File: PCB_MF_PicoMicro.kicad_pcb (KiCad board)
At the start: 2 copper layers, 36.5 x 18.5 mm, 45 parts, among them J1 Conn_01x12, J2 Conn_01x12, J3 USB_C_Receptacle_USB2.0_16P, J7 Conn_01x02_Pin, J8 Conn_01x02_Pin, SW1 SW_Push, U1 RP2040, U2 AMS1117-3.3, U4 W25Q16JVSS, Y1 X322512MSB4SI

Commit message: update production files
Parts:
- C11, C12, C13, C14, C15, C6, C9: value 100n -> 100nF
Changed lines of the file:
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@@
 			)
 		)
-		(property "Value" "100n"
+		(property "Value" "100nF"
 			(at 0 1.16 270)
 			(layer "F.Fab")
@@
 			)
 		)
-		(property "Value" "100n"
+		(property "Value" "100nF"
 			(at 0 1.16 180)
 			(layer "F.Fab")
@@
 			)
 		)
-		(property "Value" "100n"
+		(property "Value" "100nF"
 			(at 0 1.16 0)
 			(layer "F.Fab")
@@
 			)
 		)
-		(property "Value" "100n"
+		(property "Value" "100nF"
 			(at 0 1.16 0)
 			(layer "F.Fab")
@@
 			)
 		)
-		(property "Value" "100n"
+		(property "Value" "100nF"
 			(at 0 1.16 0)
 			(layer "F.Fab")
@@
 			)
 		)
+		(property "LCSC" "C25076"
+			(at 0 0 0)
+			(layer "F.SilkS")
+			(hide yes)
+			(effects
+				(font
+					(size 1.27 1.27)
+					(thickness 0.15)
+				)
+			)
+		)
 		(property ki_fp_filters "R_*")
 		(sheetname "/")
@@
 			)
 		)
-		(property "Value" "100n"
+		(property "Value" "100nF"
 			(at 0 1.16 0)
 			(layer "F.Fab")
@@
 			)
 		)
+		(property "LCSC" "C25076"
+			(at 0 0 0)
+			(layer "F.SilkS")
+			(hide yes)
+			(effects
+				(font
+					(size 1.27 1.27)
+					(thickness 0.15)
+				)
+			)
+		)
 		(property ki_fp_filters "R_*")
 		(sheetname "/")
@@
 			)
 		)
-		(property "Value" "100n"
+		(property "Value" "100nF"
 			(at 0 1.16 0)
 			(layer "F.Fab")

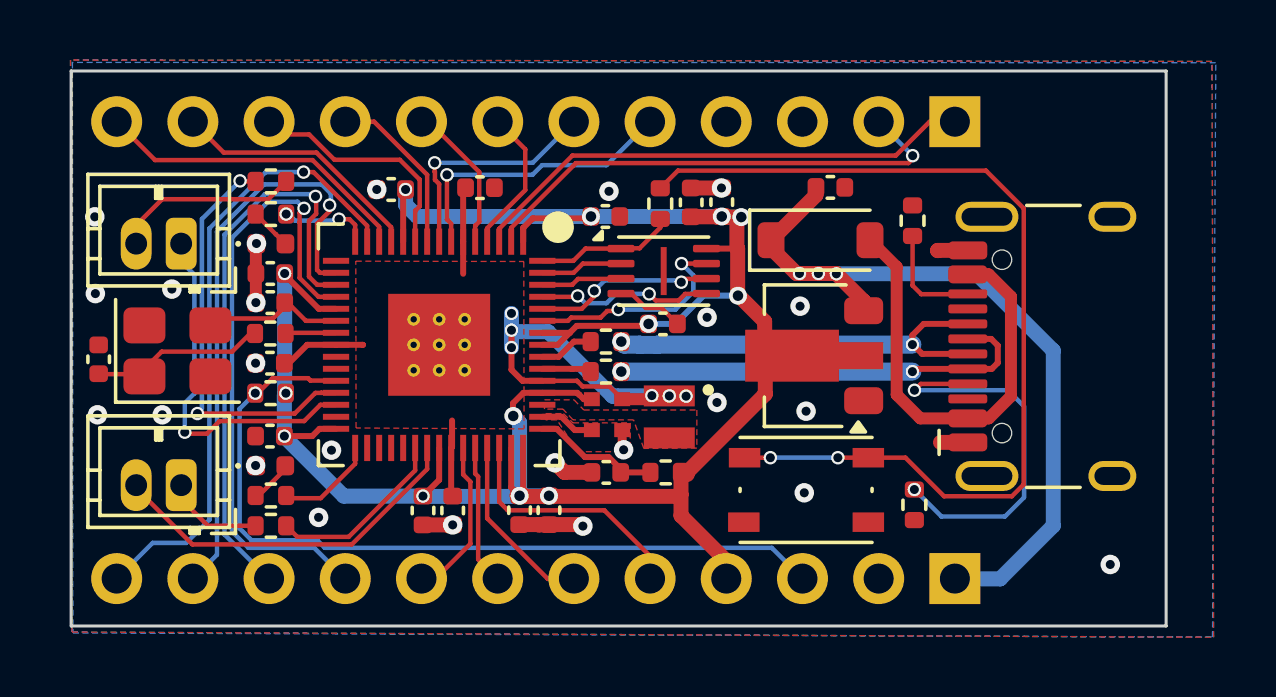
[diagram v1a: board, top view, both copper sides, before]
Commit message: swap tx line to slave, better arrangement of parts
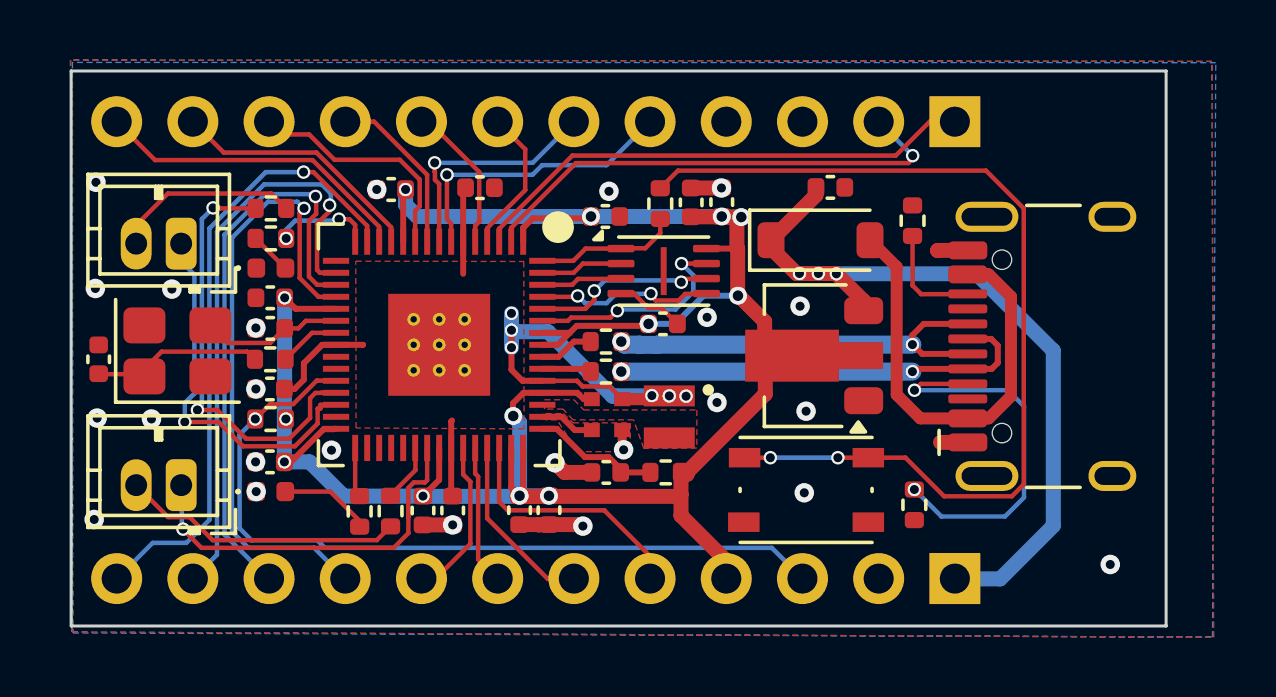
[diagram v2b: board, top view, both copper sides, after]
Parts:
- moved R12 4.02 mm to (115.9, 96.1), turned to 90 degrees
- moved R10 3.01 mm to (114.8, 96.1), turned to 90 degrees
- moved R11 0.90 mm to (111.9, 86.0)
- moved C12 0.86 mm to (111.9, 94.5)
- moved C4 0.86 mm to (111.9, 90.0)
- moved C7 0.86 mm to (111.9, 92.0)
- moved D2 0.86 mm to (111.9, 95.4)
- moved R2 0.86 mm to (111.9, 91.0)
- moved R6 0.86 mm to (111.9, 93.0)
- moved C9 0.81 mm to (111.9, 89.0)
- moved R9 0.81 mm to (111.9, 87.0)
- moved D3 0.81 mm to (111.9, 88.0)
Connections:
- J8 pad 1: Net-(J8-Pin_1) -> RX2
- J8 pad 2: RX2 -> Net-(J8-Pin_2)
- R12 pad 1: Net-(J8-Pin_1) -> Net-(J8-Pin_2)
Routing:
- net Net-(J8-Pin_2): track 0.00 -> 10.4 mm
- net TX2: track 6.12 -> 1.94 mm
- net Net-(J8-Pin_1): track 3.52 -> 0.00 mm
- net GND: track 15.8 -> 13.8 mm
- net /RP2350A/GPIO19: track 3.25 -> 1.67 mm
- net Net-(D2-A): track 1.56 -> 3.08 mm
- net RX2: track 12.6 -> 13.5 mm, vias 0 -> 1
- net TX1: track 13.8 -> 14.6 mm
- net +1V1: track 23.6 -> 24.3 mm
- net RST: track 27.6 -> 27.0 mm
- net RX1: track 12.2 -> 12.7 mm

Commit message: better positioning of parts
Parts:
- R11, R12: value 100 -> 50
- moved R6 3.63 mm to (113.8, 96.1), turned to -90 degrees
- moved D3 2.48 mm to (111.9, 85.5)
- moved R11 1.52 mm to (111.9, 87.5)
- moved C12 1.40 mm to (111.9, 93.0)
- moved D2 1.40 mm to (111.9, 94.0)
- moved R8 1.32 mm to (132.5, 85.3), turned to 0 degrees
- moved C7 0.55 mm to (111.9, 91.5)
- moved R2 0.54 mm to (111.9, 90.5)
- moved C4 0.50 mm to (111.9, 89.5)
- moved R9 0.49 mm to (111.9, 86.5)
- moved C9 0.47 mm to (111.9, 88.5)
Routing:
- net Net-(J3-CC2): track 3.61 -> 14.1 mm, vias 0 -> 2
- net RST: track 27.0 -> 32.2 mm
- net /RP2350A/~{USB_BOOT}: track 32.2 -> 35.1 mm
- net RX2: track 13.5 -> 16.3 mm
- net TX1: track 14.6 -> 12.5 mm
- net Net-(D2-A): track 3.08 -> 4.52 mm
- net Net-(J7-Pin_2): track 6.27 -> 7.60 mm
- net VIN: track 26.2 -> 25.2 mm
- net +1V1: track 24.3 -> 23.6 mm
- net Net-(J8-Pin_2): track 10.4 -> 10.9 mm
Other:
- board text removed: "D7"

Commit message: update production files
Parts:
- U1: value RP2040 -> RP2350A
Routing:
- net GND: vias 24 -> 23
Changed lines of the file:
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@@
 			)
 		)
-		(property "LCSC" "C25076"
+		(property "LCSC" "C25120"
 			(at 0 0 0)
 			(layer "F.SilkS")
@@
 			)
 		)
-		(property "LCSC" "C25076"
+		(property "LCSC" "C25120"
 			(at 0 0 90)
 			(layer "F.SilkS")
@@
 			)
 		)
-		(property "Value" "RP2040"
+		(property "Value" "RP2350A"
 			(at 0 5.55 90)
 			(layer "F.Fab")
@@
 	)
 	(gr_text "PicoMicroMS\nV1.1\n??/25"
-		(at 136.5 92.36 0)
+		(at 136.5 92.81 0)
 		(layer "B.SilkS")
 		(effects
@@
 		(size 0.65)
 		(drill 0.3)
-		(layers "F.Cu" "B.Cu")
-		(net 2)
-	)
-	(via
-		(at 139.87 97.87)
-		(size 0.65)
-		(drill 0.3)

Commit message: add SDA and SCL markings
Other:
- board text added: "SCL/D3"
- board text added: "SDA/D2"
- board text removed: "D2"
- board text removed: "D3"
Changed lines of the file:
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@@
 		)
 	)
-	(gr_text "D2"
-		(at 123.8 86.574762 270)
+	(gr_text "SDA/D2"
+		(at 123.86 90.44 270)
 		(layer "B.SilkS")
 		(effects
@@
 		)
 	)
-	(gr_text "D3"
-		(at 121.3 86.574762 270)
+	(gr_text "SCL/D3"
+		(at 121.28 90.34 270)
 		(layer "B.SilkS")
 		(effects

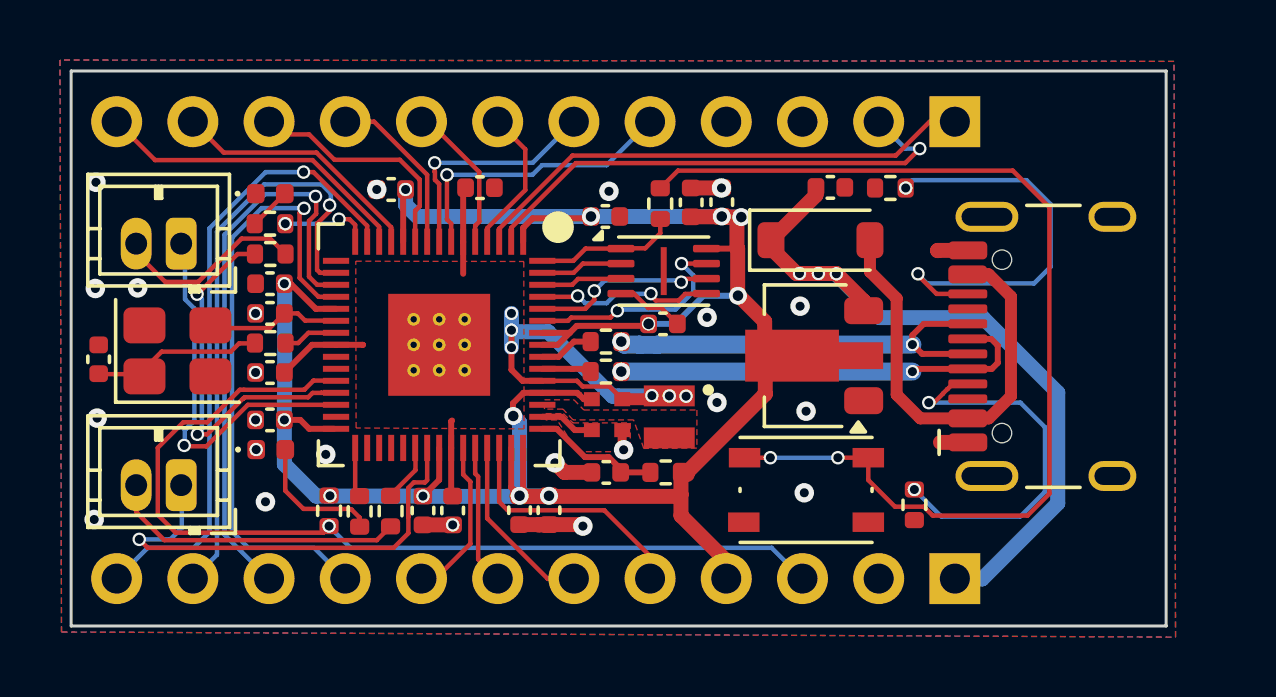
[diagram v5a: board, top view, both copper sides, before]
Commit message: use new PicoMicro Symbol and footprint
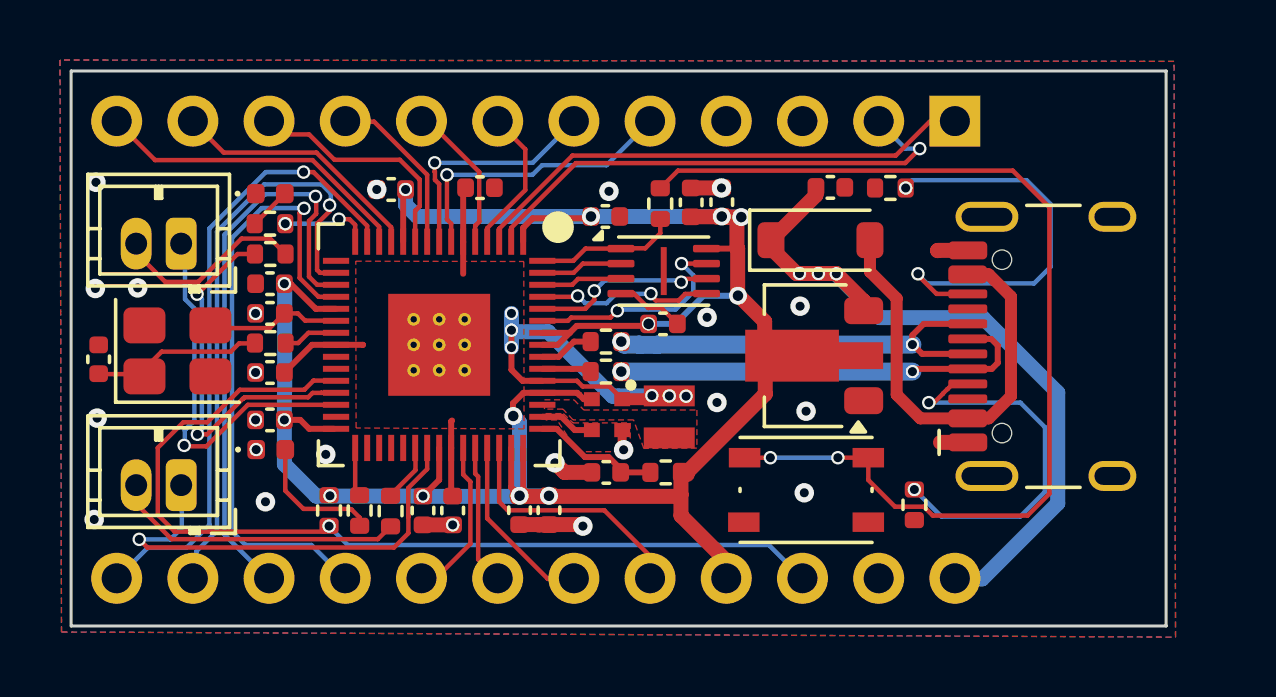
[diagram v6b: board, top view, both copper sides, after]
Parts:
- removed J2: Conn_01x12, Connector_PinHeader_2.54mm:PinHeader_1x12_P2.54mm_Vertical
- J1: value Conn_01x12 -> ~; footprint Connector_PinHeader_2.54mm:PinHeader_1x12_P2.54mm_Vertical -> _Own_Library:PicoMicro; moved to F.Cu
- turned J1 to -90 degrees

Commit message: PicoMicro footprint updated
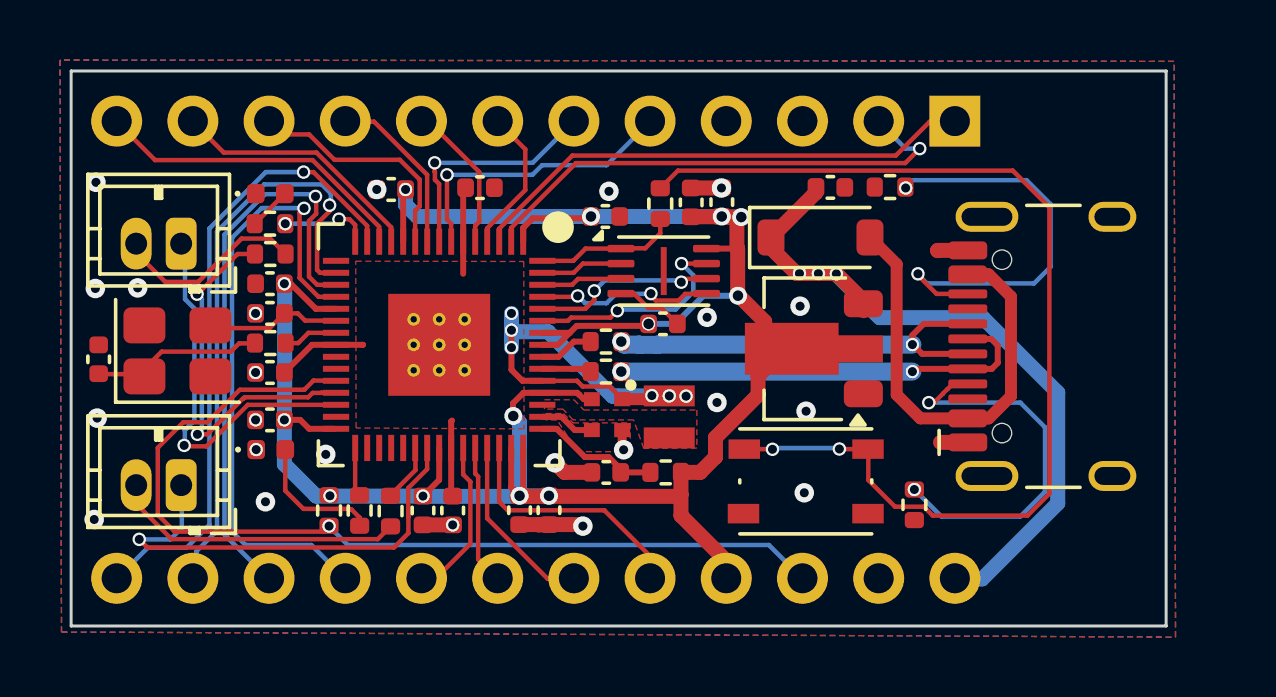
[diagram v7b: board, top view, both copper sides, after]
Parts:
- moved SW1 0.29 mm to (129.7, 95.1)
- moved U2 0.23 mm to (129.7, 90.7)
- moved D1 0.09 mm to (130.2, 87.0)
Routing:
- net 3.3V: track 82.4 -> 87.2 mm
